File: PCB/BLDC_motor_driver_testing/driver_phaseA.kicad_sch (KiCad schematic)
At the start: 20 parts, among them Q1 IRF540N, Q2 IRF540N, U2 IR2104, U3 INA240A2D, U4 LMV393

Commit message: PCB layouting...
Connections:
- net PWR_12V: now also Q1.2 (D)
- net at C7.1, D2.1 (K), U2.8 (VB): no longer Q1.2 (D)
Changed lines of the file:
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@@
+	)
+	(junction
+		(at 86.36 35.56)
+		(diameter 0)
+		(color 0 0 0 0)
 	)
 	(junction
@@
 	)
 	(junction
+		(at 66.04 93.98)
+		(diameter 0)
+		(color 0 0 0 0)
+	)
+	(junction
 		(at 83.82 85.09)
 		(diameter 0)
@@
 	)
 	(junction
-		(at 83.82 64.77)
-		(diameter 0)
-		(color 0 0 0 0)
-	)
-	(junction
 		(at 129.54 120.65)
 		(diameter 0)
@@
 	(wire
 		(pts
+			(xy 113.03 35.56) (xy 86.36 35.56)
+		)
+		(stroke
+			(width 0)
+			(type default)
+		)
+	)
+	(wire
+		(pts
 			(xy 251.46 107.95) (xy 251.46 125.73)
 		)
@@
 	(wire
 		(pts
-			(xy 113.03 64.77) (xy 113.03 69.85)
+			(xy 113.03 35.56) (xy 113.03 69.85)
 		)
 		(stroke
@@
 	(wire
 		(pts
-			(xy 66.04 92.71) (xy 66.04 96.52)
+			(xy 66.04 92.71) (xy 66.04 93.98)
 		)
 		(stroke
@@
 	(wire
 		(pts
+			(xy 55.88 93.98) (xy 66.04 93.98)
+		)
+		(stroke
+			(width 0)
+			(type default)
+		)
+	)
+	(wire
+		(pts
 			(xy 99.06 95.25) (xy 101.6 95.25)
 		)
@@
 	(wire
 		(pts
-			(xy 83.82 64.77) (xy 113.03 64.77)
-		)
-		(stroke
-			(width 0)
-			(type default)
-		)
-	)
-	(wire
-		(pts
 			(xy 80.01 48.26) (xy 73.66 48.26)
 		)
@@
 		(pts
 			(xy 86.36 45.72) (xy 86.36 48.26)
+		)
+		(stroke
+			(width 0)
+			(type default)
+		)
+	)
+	(wire
+		(pts
+			(xy 66.04 93.98) (xy 66.04 96.52)
 		)
 		(stroke
@@
 		(effects
 			(font
+				(size 1.27 1.27)
+			)
+			(justify right)
+		)
+	)
+	(hierarchical_label "GND"
+		(shape input)
+		(at 55.88 93.98 180)
+		(effects
+			(font

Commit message: Test driver layout...
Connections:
- net GND_A: now reaches C9.1, Q2.3 (S), R4.1, U3.8 (+)
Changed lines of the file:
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@@
 		)
 	)
-	(label "SD_A"
-		(at 260.35 107.95 180)
+	(label "GND_A"
+		(at 113.03 107.95 90)
 		(effects
 			(font
 				(size 1.27 1.27)
 			)
-			(justify right bottom)
+			(justify left bottom)
 		)
 	)
@@
 		)
 	)
-	(label "SD_A"
-		(at 52.07 82.55 0)
-		(effects
-			(font
-				(size 1.27 1.27)
-			)
-			(justify left bottom)
-		)
-	)
 	(label "VISENSE_A"
 		(at 156.21 115.57 0)
@@
 		)
 	)
+	(global_label "SD_A"
+		(shape input)
+		(at 260.35 107.95 0)
+		(fields_autoplaced yes)
+		(effects
+			(font
+				(size 1.27 1.27)
+			)
+			(justify left)
+		)
+		(property "Intersheetrefs" "${INTERSHEET_REFS}"
+			(at 267.8709 107.95 0)
+			(effects
+				(font
+					(size 1.27 1.27)
+				)
+				(justify left)
+				(hide yes)
+			)
+		)
+	)

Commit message: Getting closer to finish 2 ;)
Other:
- moved on the sheet: R7
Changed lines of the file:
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@@
+	)
+	(junction
+		(at 49.53 82.55)
+		(diameter 0)
+		(color 0 0 0 0)
 	)
 	(junction
@@
 	)
 	(junction
-		(at 251.46 107.95)
-		(diameter 0)
-		(color 0 0 0 0)
-	)
-	(junction
 		(at 66.04 93.98)
 		(diameter 0)
@@
 	)
 	(junction
+		(at 254 107.95)
+		(diameter 0)
+		(color 0 0 0 0)
+	)
+	(junction
 		(at 209.55 110.49)
 		(diameter 0)
@@
 	(wire
 		(pts
-			(xy 247.65 107.95) (xy 251.46 107.95)
-		)
-		(stroke
-			(width 0)
-			(type default)
-		)
-	)
-	(wire
-		(pts
-			(xy 43.18 82.55) (xy 58.42 82.55)
+			(xy 247.65 107.95) (xy 254 107.95)
+		)
+		(stroke
+			(width 0)
+			(type default)
+		)
+	)
+	(wire
+		(pts
+			(xy 43.18 82.55) (xy 49.53 82.55)
+		)
+		(stroke
+			(width 0)
+			(type default)
+		)
+	)
+	(wire
+		(pts
+			(xy 43.18 86.36) (xy 49.53 86.36)
 		)
 		(stroke
@@
 	(wire
 		(pts
+			(xy 49.53 86.36) (xy 49.53 82.55)
+		)
+		(stroke
+			(width 0)
+			(type default)
+		)
+	)
+	(wire
+		(pts
 			(xy 113.03 35.56) (xy 86.36 35.56)
 		)
@@
 	(wire
 		(pts
-			(xy 251.46 107.95) (xy 251.46 125.73)
+			(xy 254 107.95) (xy 254 125.73)
+		)
+		(stroke
+			(width 0)
+			(type default)
+		)
+	)
+	(wire
+		(pts
+			(xy 254 107.95) (xy 259.08 107.95)
 		)
 		(stroke
@@
 	(wire
 		(pts
-			(xy 251.46 107.95) (xy 260.35 107.95)
-		)
-		(stroke
-			(width 0)
-			(type default)
-		)
-	)
-	(wire
-		(pts
 			(xy 83.82 83.82) (xy 83.82 85.09)
 		)
@@
 	(wire
 		(pts
-			(xy 251.46 104.14) (xy 251.46 107.95)
+			(xy 254 104.14) (xy 254 107.95)
 		)
 		(stroke
@@
 	(wire
 		(pts
+			(xy 49.53 82.55) (xy 58.42 82.55)
+		)
+		(stroke
+			(width 0)
+			(type default)
+		)
+	)
+	(wire
+		(pts
 			(xy 209.55 93.98) (xy 209.55 99.06)
 		)
@@
 	(wire
 		(pts
-			(xy 251.46 93.98) (xy 251.46 96.52)
+			(xy 254 93.98) (xy 254 96.52)
 		)
 		(stroke
@@
 	(wire
 		(pts
-			(xy 231.14 125.73) (xy 251.46 125.73)
+			(xy 231.14 125.73) (xy 254 125.73)
 		)
 		(stroke
@@
 	(wire
 		(pts
-			(xy 209.55 93.98) (xy 251.46 93.98)
+			(xy 209.55 93.98) (xy 254 93.98)
 		)
 		(stroke
@@
 	(global_label "SD_A"
 		(shape input)
-		(at 260.35 107.95 0)
+		(at 259.08 107.95 0)
 		(fields_autoplaced yes)
 		(effects
@@
 		)
 		(property "Intersheetrefs" "${INTERSHEET_REFS}"
-			(at 267.8709 107.95 0)
+			(at 266.6009 107.95 0)
 			(effects
 				(font
@@
 				)
 				(justify left)
+				(hide yes)
+			)
+		)
+	)
+	(global_label "SD_A"
+		(shape input)
+		(at 43.18 86.36 180)
+		(fields_autoplaced yes)
+		(effects
+			(font
+				(size 1.27 1.27)
+			)
+			(justify right)
+		)
+		(property "Intersheetrefs" "${INTERSHEET_REFS}"
+			(at 35.6591 86.36 0)
+			(effects
+				(font
+					(size 1.27 1.27)
+				)
+				(justify right)
 				(hide yes)
 			)
@@
 	(symbol
 		(lib_id "Device:R")
-		(at 251.46 100.33 180)
+		(at 254 100.33 180)
 		(unit 1)
 		(exclude_from_sim no)
@@
 		(dnp no)
 		(property "Reference" "R7"
-			(at 253.492 99.06 0)
+			(at 256.032 99.06 0)
 			(effects
 				(font
@@
 		)
 		(property "Value" "4.7K"
-			(at 253.492 101.6 0)
+			(at 256.032 101.6 0)
 			(effects
 				(font
@@
 		)
 		(property "Footprint" "Resistor_SMD:R_0805_2012Metric_Pad1.20x1.40mm_HandSolder"
-			(at 253.238 100.33 90)
+			(at 255.778 100.33 90)
 			(effects
 				(font
@@
 		)
 		(property "Datasheet" "~"
-			(at 251.46 100.33 0)
+			(at 254 100.33 0)
 			(effects
 				(font
@@
 		)
 		(property "Description" "Resistor"
-			(at 251.46 100.33 0)
-			(effects
-				(font
+			(at 254 100.33 0)
+			(effects
+				(font

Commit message: Almost there 0_0
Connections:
- net GND: no longer R7.1, U2.3 (~{SD}), U4.1
- new net SD_A: R7.1, U2.3 (~{SD}), U4.1
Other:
- moved on the sheet: R7
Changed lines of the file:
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@@
+	)
+	(junction
+		(at 252.73 107.95)
+		(diameter 0)
+		(color 0 0 0 0)
 	)
 	(junction
@@
 	)
 	(junction
-		(at 231.14 125.73)
-		(diameter 0)
-		(color 0 0 0 0)
-	)
-	(junction
-		(at 49.53 82.55)
-		(diameter 0)
-		(color 0 0 0 0)
-	)
-	(junction
 		(at 83.82 72.39)
 		(diameter 0)
@@
 	)
 	(junction
-		(at 254 107.95)
-		(diameter 0)
-		(color 0 0 0 0)
-	)
-	(junction
 		(at 209.55 110.49)
 		(diameter 0)
@@
 	(wire
 		(pts
-			(xy 247.65 107.95) (xy 254 107.95)
-		)
-		(stroke
-			(width 0)
-			(type default)
-		)
-	)
-	(wire
-		(pts
-			(xy 43.18 82.55) (xy 49.53 82.55)
-		)
-		(stroke
-			(width 0)
-			(type default)
-		)
-	)
-	(wire
-		(pts
-			(xy 43.18 86.36) (xy 49.53 86.36)
+			(xy 247.65 107.95) (xy 252.73 107.95)
 		)
 		(stroke
@@
 	(wire
 		(pts
-			(xy 49.53 86.36) (xy 49.53 82.55)
-		)
-		(stroke
-			(width 0)
-			(type default)
-		)
-	)
-	(wire
-		(pts
 			(xy 113.03 35.56) (xy 86.36 35.56)
 		)
@@
 	(wire
 		(pts
-			(xy 254 107.95) (xy 254 125.73)
-		)
-		(stroke
-			(width 0)
-			(type default)
-		)
-	)
-	(wire
-		(pts
-			(xy 254 107.95) (xy 259.08 107.95)
-		)
-		(stroke
-			(width 0)
-			(type default)
-		)
-	)
-	(wire
-		(pts
 			(xy 113.03 110.49) (xy 129.54 110.49)
 		)
@@
 	(wire
 		(pts
+			(xy 252.73 107.95) (xy 262.89 107.95)
+		)
+		(stroke
+			(width 0)
+			(type default)
+		)
+	)
+	(wire
+		(pts
 			(xy 143.51 127) (xy 143.51 123.19)
 		)
@@
 	(wire
 		(pts
-			(xy 231.14 125.73) (xy 209.55 125.73)
-		)
-		(stroke
-			(width 0)
-			(type default)
-		)
-	)
-	(wire
-		(pts
 			(xy 66.04 92.71) (xy 66.04 93.98)
 		)
@@
 	(wire
 		(pts
-			(xy 231.14 125.73) (xy 231.14 128.27)
-		)
-		(stroke
-			(width 0)
-			(type default)
-		)
-	)
-	(wire
-		(pts
 			(xy 113.03 120.65) (xy 113.03 125.73)
 		)
@@
 	(wire
 		(pts
-			(xy 43.18 80.01) (xy 58.42 80.01)
+			(xy 49.53 80.01) (xy 58.42 80.01)
 		)
 		(stroke
@@
 	(wire
 		(pts
-			(xy 254 104.14) (xy 254 107.95)
+			(xy 252.73 104.14) (xy 252.73 107.95)
 		)
 		(stroke
@@
 	(wire
 		(pts
-			(xy 209.55 125.73) (xy 209.55 121.92)
+			(xy 209.55 121.92) (xy 209.55 127)
 		)
 		(stroke
@@
 	(wire
 		(pts
-			(xy 254 93.98) (xy 254 96.52)
+			(xy 252.73 93.98) (xy 252.73 96.52)
 		)
 		(stroke
@@
 	(wire
 		(pts
-			(xy 231.14 125.73) (xy 254 125.73)
-		)
-		(stroke
-			(width 0)
-			(type default)
-		)
-	)
-	(wire
-		(pts
 			(xy 101.6 95.25) (xy 105.41 95.25)
 		)
@@
 	(wire
 		(pts
-			(xy 209.55 93.98) (xy 254 93.98)
+			(xy 209.55 93.98) (xy 252.73 93.98)
 		)
 		(stroke
@@
 		)
 	)
+	(label "SD_A"
+		(at 53.34 82.55 0)
+		(effects
+			(font
+				(size 1.27 1.27)
+			)
+			(justify left bottom)
+		)
+	)
+	(label "SD_A"
+		(at 262.89 107.95 180)
+		(effects
+			(font
+				(size 1.27 1.27)
+			)
+			(justify right bottom)
+		)
+	)
 	(label "VISENSE_A"
 		(at 156.21 115.57 0)
@@
 		)
 	)
-	(global_label "SD_A"
+	(hierarchical_label "SD_A"
 		(shape input)
-		(at 259.08 107.95 0)
-		(fields_autoplaced yes)
+		(at 49.53 82.55 180)
 		(effects
 			(font
 				(size 1.27 1.27)
 			)
-			(justify left)
-		)
-		(property "Intersheetrefs" "${INTERSHEET_REFS}"
-			(at 266.6009 107.95 0)
-			(effects
-				(font
-					(size 1.27 1.27)
-				)
-				(justify left)
-				(hide yes)
-			)
-		)
-	)
-	(global_label "SD_A"
-		(shape input)
-		(at 43.18 86.36 180)
-		(fields_autoplaced yes)
-		(effects
-			(font
-				(size 1.27 1.27)
-			)
-			(justify right)
-		)
-		(property "Intersheetrefs" "${INTERSHEET_REFS}"
-			(at 35.6591 86.36 0)
-			(effects
-				(font
-					(size 1.27 1.27)
-				)
-				(justify right)
-				(hide yes)
-			)
-		)
-	)
-	(hierarchical_label "SD_A"
-		(shape input)
-		(at 43.18 82.55 180)
-		(effects
-			(font
-				(size 1.27 1.27)
-			)
 			(justify right)
 		)
@@
 	(hierarchical_label "PWM_IN_A"
 		(shape input)
-		(at 43.18 80.01 180)
+		(at 49.53 80.01 180)
 		(effects
 			(font
@@
 	(symbol
 		(lib_id "power:GND")
-		(at 231.14 128.27 0)
+		(at 209.55 127 0)
 		(unit 1)
 		(exclude_from_sim no)
@@
 		(dnp no)
 		(property "Reference" "#PWR019"
-			(at 231.14 134.62 0)
+			(at 209.55 133.35 0)
 			(effects
 				(font
@@
 		)
 		(property "Value" "GND"
-			(at 231.14 132.334 0)
+			(at 209.55 131.064 0)
 			(effects
 				(font
@@
 		)
 		(property "Footprint" ""
-			(at 231.14 128.27 0)
+			(at 209.55 127 0)
 			(effects
 				(font
@@
 		)
 		(property "Datasheet" ""
-			(at 231.14 128.27 0)
+			(at 209.55 127 0)
 			(effects
 				(font
@@
 		)
 		(property "Description" "Power symbol creates a global label with name \"GND\" , ground"
-			(at 231.14 128.27 0)
+			(at 209.55 127 0)
 			(effects
 				(font
@@
 	(symbol
 		(lib_id "Device:R")
-		(at 254 100.33 180)
+		(at 252.73 100.33 180)
 		(unit 1)
 		(exclude_from_sim no)
@@
 		(dnp no)
 		(property "Reference" "R7"
-			(at 256.032 99.06 0)
+			(at 254.762 99.06 0)
 			(effects
 				(font
@@
 		)
 		(property "Value" "4.7K"
-			(at 256.032 101.6 0)
+			(at 254.762 101.6 0)
 			(effects
 				(font
@@
 		)
 		(property "Footprint" "Resistor_SMD:R_0805_2012Metric_Pad1.20x1.40mm_HandSolder"
-			(at 255.778 100.33 90)
+			(at 254.508 100.33 90)
 			(effects
 				(font
@@
 		)
 		(property "Datasheet" "~"
-			(at 254 100.33 0)
+			(at 252.73 100.33 0)
 			(effects
 				(font
@@
 		)
 		(property "Description" "Resistor"
-			(at 254 100.33 0)
-			(effects
-				(font
+			(at 252.73 100.33 0)
+			(effects
+				(font

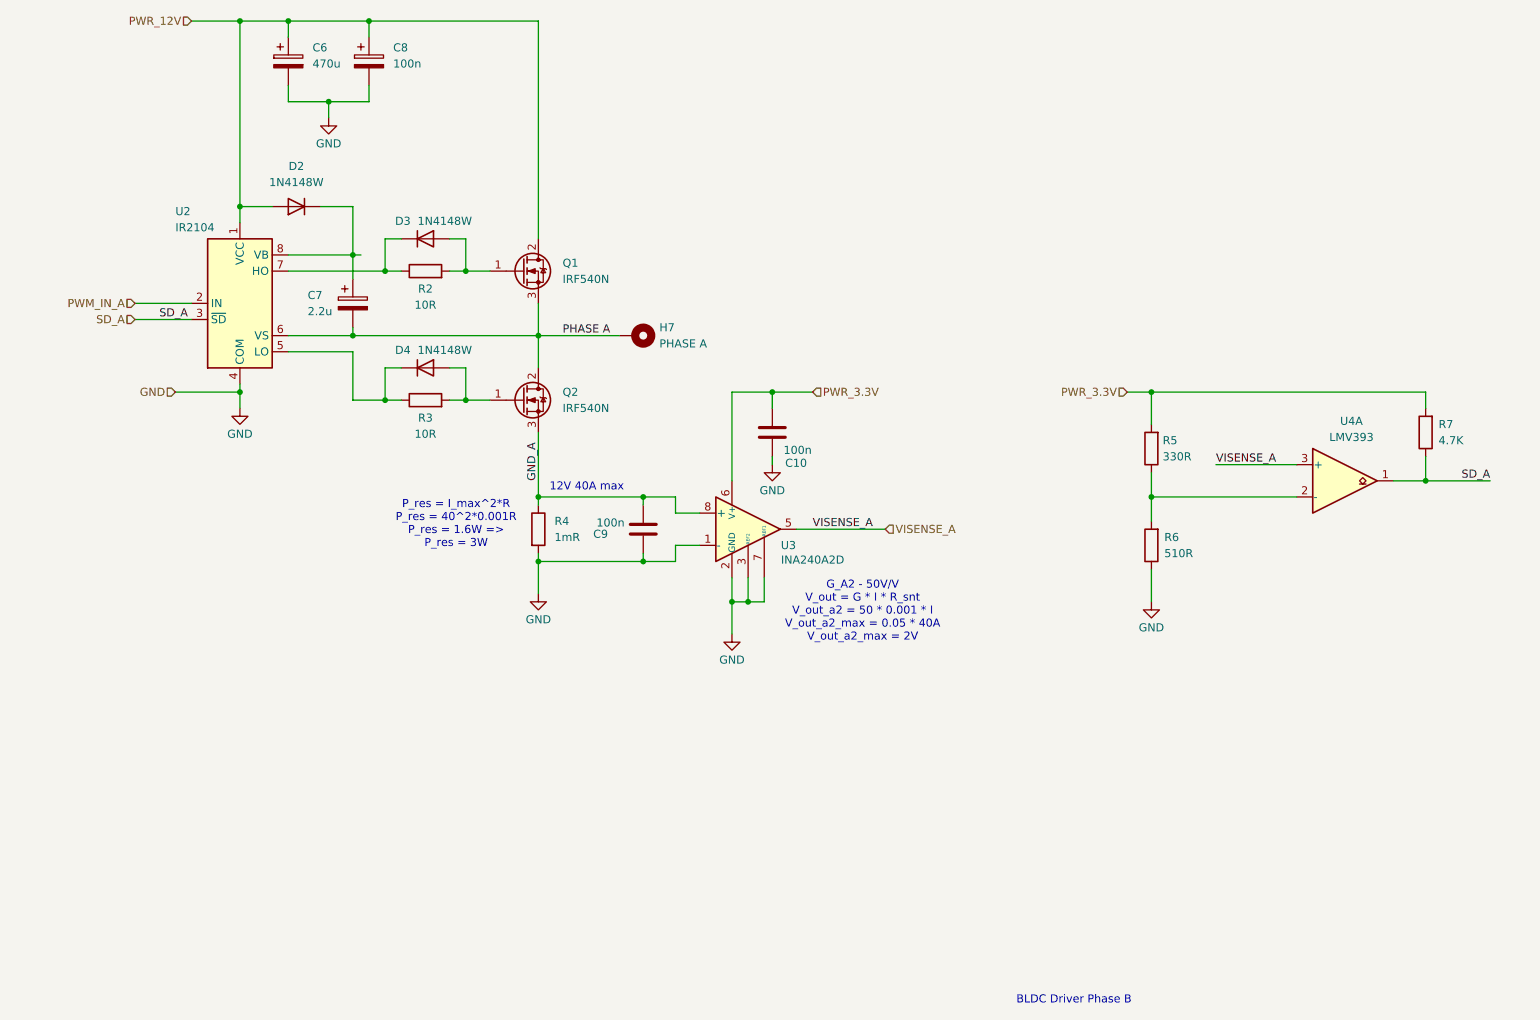
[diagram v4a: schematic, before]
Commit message: Gnd pours required, signal line EMI checking
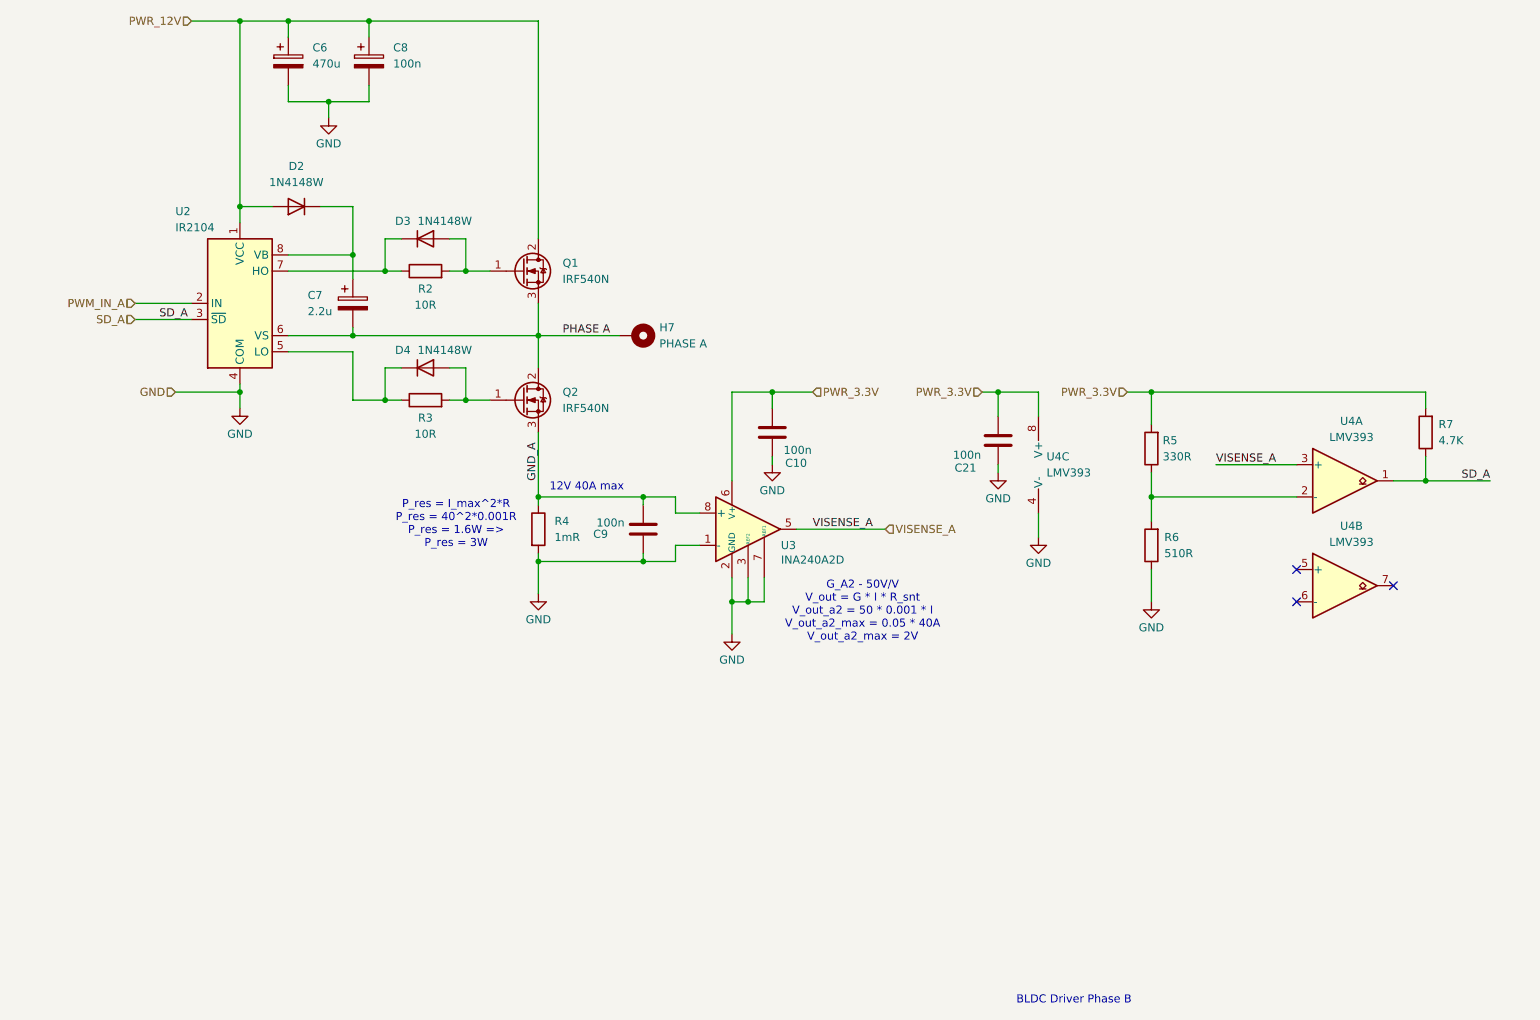
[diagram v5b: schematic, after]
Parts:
- added C21: 100n, Capacitor_SMD:C_0805_2012Metric_Pad1.18x1.45mm_HandSolder, symbol Device:C
- added unit 2 of U4
- added unit 3 of U4
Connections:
- net GND: now also C21.2, U4.4 (V-)
- net PWR_3.3V: now also C21.1, U4.8 (V+)
- no-connect marks 0 -> 3

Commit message: more changes
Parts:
- C7: value 2.2u -> 22u
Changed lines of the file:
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@@
 			)
 		)
-		(property "Value" "2.2u"
+		(property "Value" "22u"
 			(at 76.708 81.28 0)
 			(effects

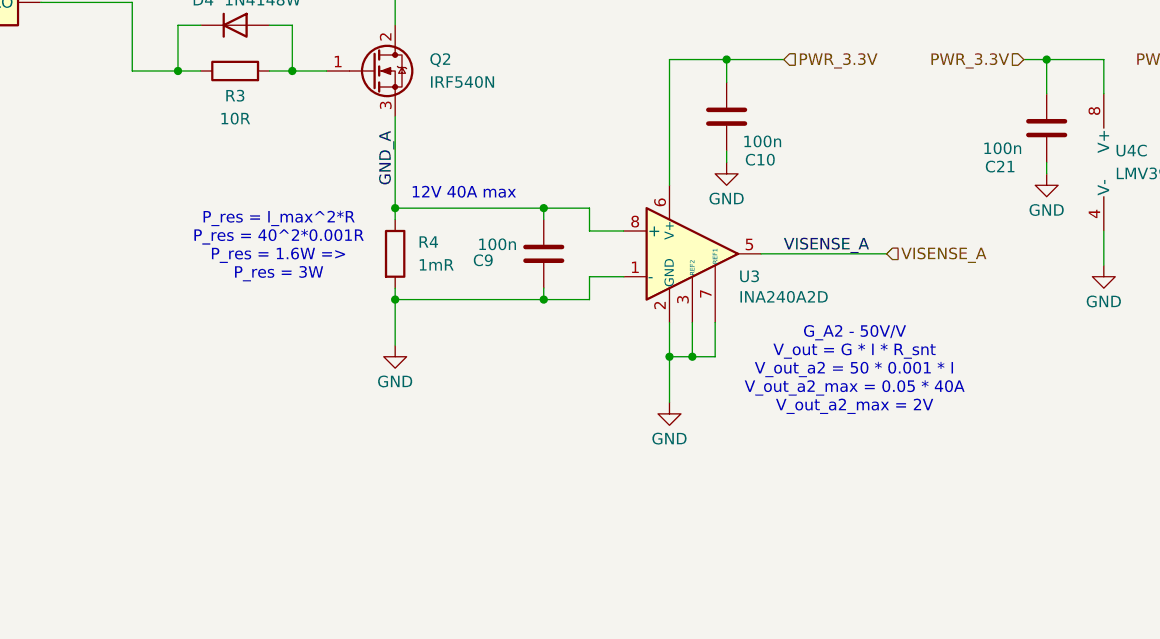
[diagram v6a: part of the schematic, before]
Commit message: small corrections for test driver
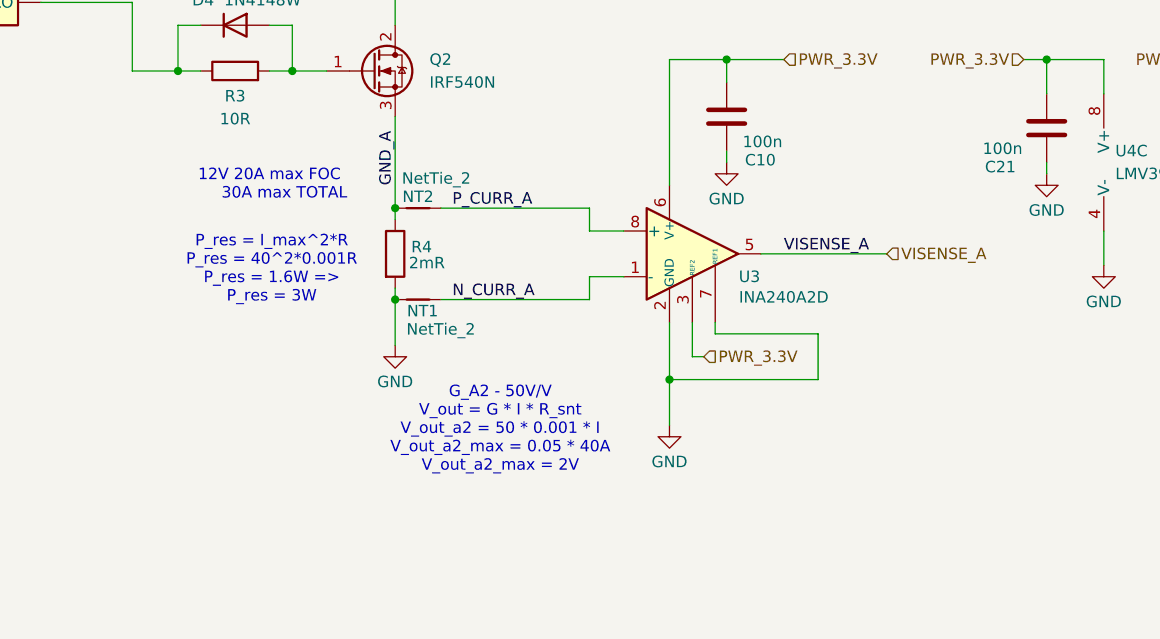
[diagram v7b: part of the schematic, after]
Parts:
- removed C9: 100n, Capacitor_SMD:C_0805_2012Metric_Pad1.18x1.45mm_HandSolder, symbol Device:C
- added NT1, NT2: NetTie_2, NetTie:NetTie-2_SMD_Pad0.5mm, symbol Device:NetTie_2
- R4: value 1mR -> 2mR
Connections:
- net GND: now also NT1.2; no longer U3.1 (-), U3.3 (REF2)
- net GND_A: now also NT2.1; no longer U3.8 (+)
- net PWR_3.3V: now also U3.3 (REF2)
- new net N_CURR_A: NT1.1, U3.1 (-)
- new net P_CURR_A: NT2.2, U3.8 (+)
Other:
- note added: "12V 20A max FOC 30A max TOTAL"
- note removed: "12V 40A max"

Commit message: getting there...
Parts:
- R4: value 2mR -> 3mR
- R5: value 330R -> 1K
- R6: value 510R -> 10K
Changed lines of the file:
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@@
 			)
 		)
-		(property "Value" "330R"
+		(property "Value" "1K"
 			(at 211.328 104.14 0)
 			(effects
@@
 			)
 		)
-		(property "Value" "2mR"
+		(property "Value" "3mR"
 			(at 114.554 116.586 0)
 			(effects
@@
 			)
 		)
-		(property "Value" "510R"
+		(property "Value" "10K"
 			(at 211.582 119.38 0)
 			(effects
